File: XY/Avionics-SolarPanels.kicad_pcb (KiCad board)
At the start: 4 copper layers, 82 x 100 mm, 202 parts, among them J1 200528-0100, J2 200528-0100, Q1 IRLML2803, Q17 NX3008NBKS, Q18 MBT2222ADW1T1, Q19 NX3008NBKS, Q2 SiRA99DP, Q20 MBT2222ADW1T1, Q21 NX3008NBKS, Q22 MBT2222ADW1T1, Q23 NX3008NBKS, Q24 MBT2222ADW1T1, Q25 NX3008NBKS, Q26 MBT2222ADW1T1, Q3 SiRA99DP, Q4 SiRA99DP, Q5 SiRA99DP, Q7 NX3008NBKS, Q8 MBT2222ADW1T1, U1 LTC4412xS6, U10 LTC3130, U11 LTC3130, U12 LTC3130, U13 ADM1176-1ARMZ-R7, U2 DRV8235RTER, U4 LTC4412xS6, U5 OPT4003DNPRQ1, U6 USBLC6-2P6, U8 LTC4412xS6

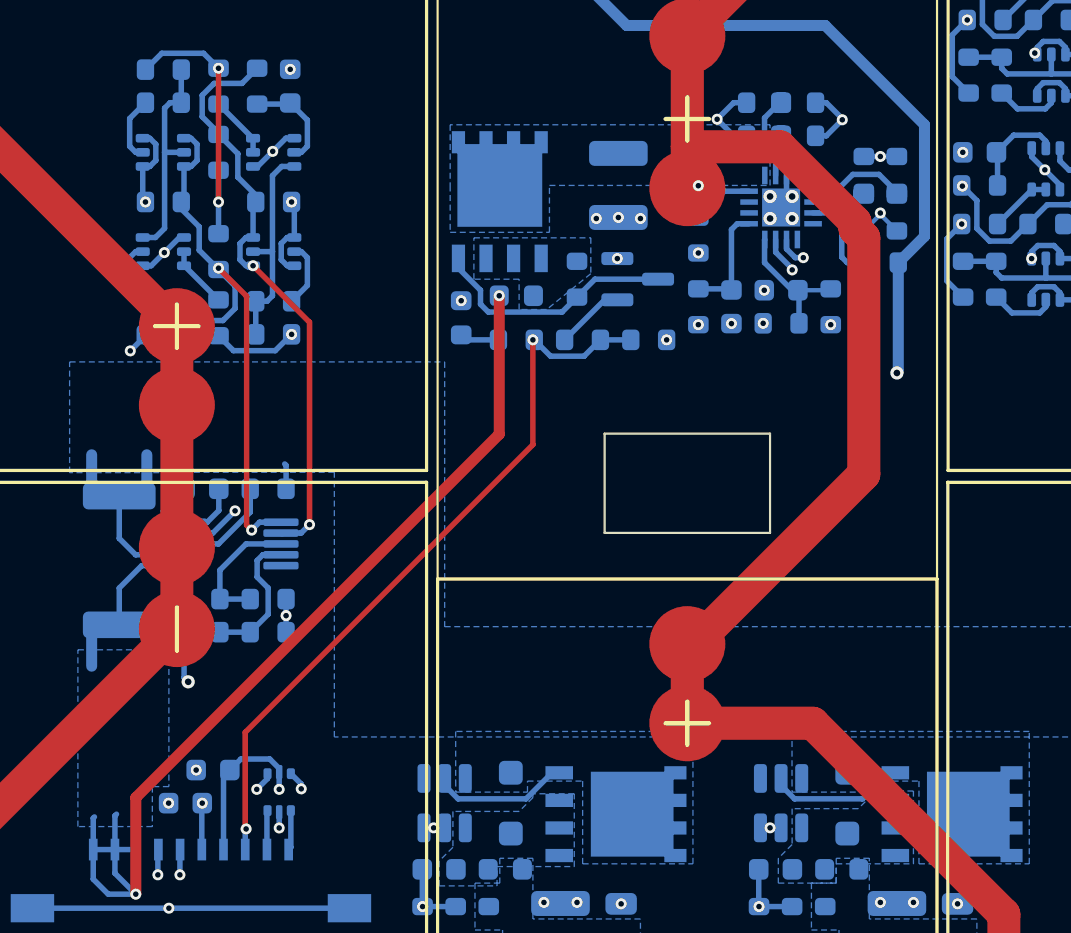
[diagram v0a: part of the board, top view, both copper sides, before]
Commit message: Increased usbc connnector size
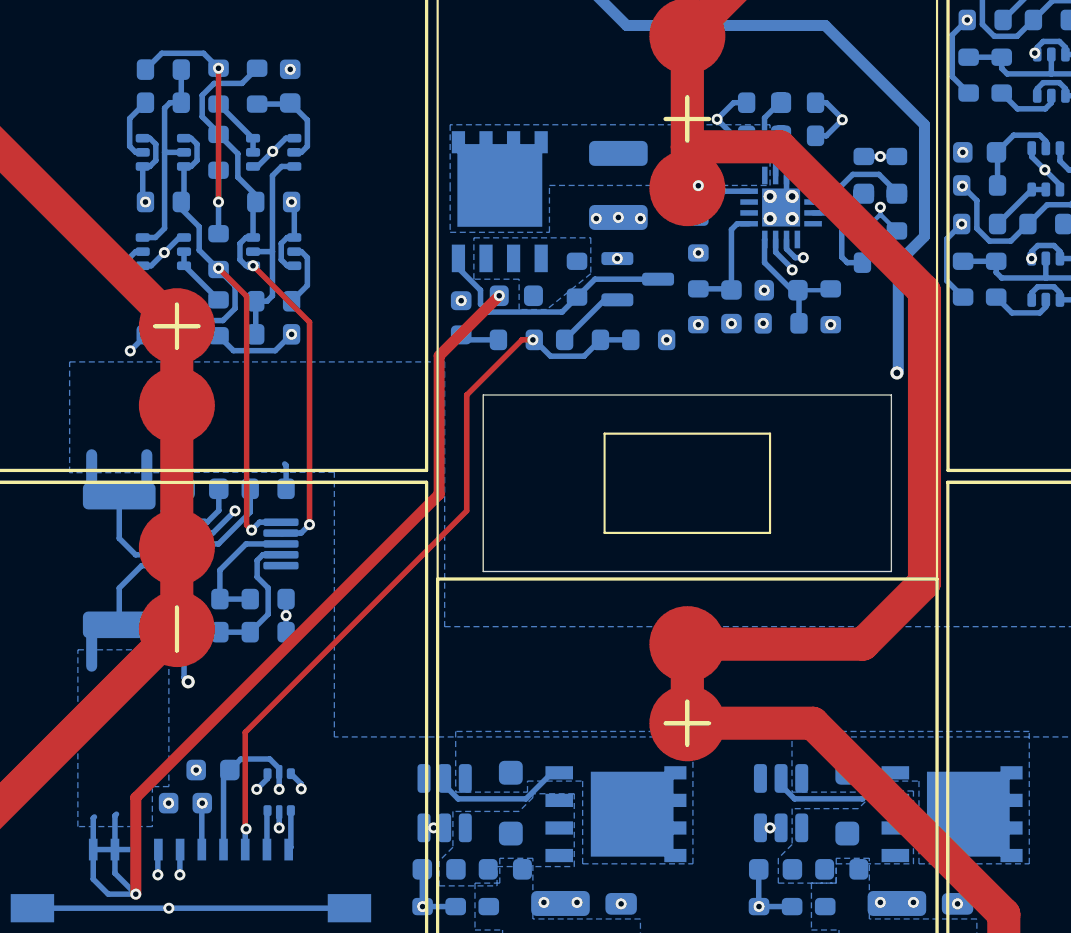
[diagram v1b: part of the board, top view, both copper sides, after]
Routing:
- net Net-(D3-K): track 140.4 -> 147.2 mm
- net PERI_3V3: track 99.6 -> 98.8 mm
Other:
- outline, holes or cut-outs redrawn
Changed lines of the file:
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@@
 		(tags "capacitor")
 		(property "Reference" "C22"
-			(at 3.302 -0.254 90)
+			(at 2.54 0 90)
 			(layer "B.SilkS")
 			(effects
@@
 		(tags "capacitor")
 		(property "Reference" "C28"
-			(at 0 -3.302 0)
+			(at 0 -2.794 0)
 			(layer "B.SilkS")
 			(effects
@@
 		(tags "resistor")
 		(property "Reference" "R53"
-			(at 3.048 0 90)
+			(at 2.54 0 90)
 			(layer "B.SilkS")
 			(effects
@@
 		(tags "resistor")
 		(property "Reference" "R32"
-			(at 3.302 -0.254 90)
+			(at 2.54 0 90)
 			(layer "B.SilkS")
 			(effects
@@
 		(tags "resistor")
 		(property "Reference" "R37"
-			(at 0 -1.778 0)
+			(at 0 -1.524 0)
 			(layer "B.SilkS")
 			(effects
@@
 		(tags "resistor")
 		(property "Reference" "R52"
-			(at 0 3.302 0)
+			(at 0 2.286 0)
 			(layer "B.SilkS")
 			(effects
@@
 		(tags "resistor")
 		(property "Reference" "R39"
-			(at 0 -1.778 0)
+			(at 0 -1.524 0)
 			(layer "B.SilkS")
 			(effects
@@
 	)
 	(gr_line
-		(start 156.21 100.584)
-		(end 148.59 100.584)
+		(start 161.798 98.806)
+		(end 143.002 98.806)
 		(stroke
 			(width 0.05)
@@
 	)
 	(gr_line
-		(start 148.59 100.584)
-		(end 148.59 105.156)
+		(start 143.002 98.806)
+		(end 143.002 106.934)
 		(stroke
 			(width 0.05)
@@
 	)
 	(gr_line
-		(start 148.59 105.156)
-		(end 156.21 105.156)
+		(start 143.002 106.934)
+		(end 161.798 106.934)
 		(stroke
 			(width 0.05)
@@
 	)
 	(gr_line
-		(start 156.21 105.156)
-		(end 156.21 100.584)
+		(start 161.798 106.934)
+		(end 161.798 98.806)
 		(stroke
 			(width 0.05)
@@
 	)
 	(via
-		(at 161.29 90.424)
+		(at 161.290001 90.157072)
 		(size 0.508)
 		(drill 0.254)
@@
 	)
 	(segment
+		(start 161.290001 90.157072)
+		(end 161.29 90.157073)
+		(width 0.2032)
+		(layer "B.Cu")
+		(net 40)
+	)
+	(segment
 		(start 161.29 90.487)
 		(end 160.528 91.249)
@@
 	)
 	(segment
-		(start 161.29 90.424)
-		(end 161.29 90.487)
-		(width 0.2032)
-		(layer "B.Cu")
-		(net 40)
-	)
-	(segment
 		(start 177.355 90.932)
 		(end 178.04386 90.24314)
@@
 	)
 	(segment
+		(start 161.29 90.157073)
+		(end 161.29 90.487)
+		(width 0.2032)
+		(layer "B.Cu")
+		(net 40)
+	)
+	(segment
 		(start 178.04386 88.31886)
 		(end 177.292 87.567)
@@
 	)
 	(segment
-		(start 152.703846 110.2786)
-		(end 160.528 102.454446)
-		(width 1.524)
-		(layer "F.Cu")
-		(net 46)
-	)
-	(segment
-		(start 160.528 102.454446)
-		(end 160.528 91.564776)
+		(start 160.4854 110.2786)
+		(end 163.322 107.442)
 		(width 1.524)
 		(layer "F.Cu")
@@
 	)
 	(segment
-		(start 160.528 91.564776)
-		(end 160.12414 91.160916)
-		(width 1.524)
-		(layer "F.Cu")
-		(net 46)
-	)
-	(segment
 		(start 167.728 147.574)
 		(end 166.978 146.824)
@@
 	)
 	(segment
-		(start 152.4 87.376)
-		(end 152.4 82.2786)
+		(start 152.4 110.2786)
+		(end 160.4854 110.2786)
 		(width 1.524)
 		(layer "F.Cu")
@@
 	)
 	(segment
-		(start 160.12414 91.160916)
-		(end 160.12414 90.839522)
+		(start 152.4 87.376)
+		(end 152.4 82.2786)
 		(width 1.524)
 		(layer "F.Cu")
@@
 	)
 	(segment
-		(start 160.12414 90.839522)
-		(end 156.660618 87.376)
+		(start 163.322 107.442)
+		(end 163.322 94.037382)
+		(width 1.524)
+		(layer "F.Cu")
+		(net 46)
+	)
+	(segment
+		(start 156.660618 87.376)
+		(end 152.4 87.376)
 		(width 1.524)
 		(layer "F.Cu")
@@
 	)
 	(segment
-		(start 156.660618 87.376)
-		(end 152.4 87.376)
+		(start 163.322 94.037382)
+		(end 156.660618 87.376)
 		(width 1.524)
 		(layer "F.Cu")
@@
 	)
 	(segment
-		(start 152.4 110.2786)
-		(end 152.703846 110.2786)
-		(width 1.524)
-		(layer "F.Cu")
-		(net 46)
-	)
-	(segment
 		(start 166.978 146.824)
 		(end 166.978 122.723026)
@@
 	)
 	(segment
-		(start 149.098 97.79)
-		(end 145.034 101.854)
+		(start 162.052 97.79)
+		(end 162.56 98.298)
 		(width 0.508)
 		(layer "In2.Cu")
@@
 	)
 	(segment
-		(start 140.988553 118.0815)
-		(end 130.5405 118.0815)
+		(start 162.56 107.442)
+		(end 151.9205 118.0815)
 		(width 0.508)
 		(layer "In2.Cu")
@@
 	)
 	(segment
-		(start 145.034 114.046)
-		(end 140.993526 118.086474)
+		(start 162.56 98.298)
+		(end 162.56 107.442)
 		(width 0.508)
 		(layer "In2.Cu")
@@
 	)
 	(segment
-		(start 140.993526 118.086474)
-		(end 140.988553 118.0815)
+		(start 151.9205 118.0815)
+		(end 130.5405 118.0815)
 		(width 0.508)
 		(layer "In2.Cu")
@@
 	)
 	(segment
-		(start 145.034 101.854)
-		(end 145.034 114.046)
-		(width 0.508)
-		(layer "In2.Cu")
-		(net 48)
-	)
-	(segment
-		(start 162.052 97.79)
-		(end 149.098 97.79)
-		(width 0.508)
-		(layer "In2.Cu")
-		(net 48)
-	)
-	(segment
 		(start 145.796 77.978)
 		(end 149.606 81.788)
@@
 	)
 	(segment
-		(start 127 117.348)
-		(end 143.7385 100.6095)
+		(start 140.97 97.0025)
+		(end 143.7385 94.234)
 		(width 0.508)
 		(layer "F.Cu")
@@
 	)
 	(segment
-		(start 127 121.793)
-		(end 127 117.348)
+		(start 140.97 103.378)
+		(end 140.97 97.0025)
 		(width 0.508)
 		(layer "F.Cu")
@@
 	)
 	(segment
-		(start 143.7385 100.6095)
-		(end 143.7385 94.234)
+		(start 127 117.348)
+		(end 140.97 103.378)
+		(width 0.508)
+		(layer "F.Cu")
+		(net 53)
+	)
+	(segment
+		(start 127 121.793)
+		(end 127 117.348)
 		(width 0.508)
 		(layer "F.Cu")
@@
 	(segment
 		(start 132.04 114.34)
-		(end 145.288 101.092)
+		(end 142.24 104.14)
+		(width 0.254)
+		(layer "F.Cu")
+		(net 101)
+	)
+	(segment
+		(start 142.24 104.14)
+		(end 142.24 98.806)
 		(width 0.254)
 		(layer "F.Cu")
@@
 	)
 	(segment
-		(start 145.288 101.092)
+		(start 144.78 96.266)
 		(end 145.288 96.266)
 		(width 0.254)
 		(layer "F.Cu")
+		(net 101)
+	)
+	(segment
+		(start 142.24 98.806)
+		(end 144.78 96.266)
+		(width 0.254)
+		(layer "F.Cu")

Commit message: Routing modifications
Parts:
- removed C36: 0.1uF, Capacitor_SMD:C_0603_1608Metric
- moved R102 4.82 mm to (152.9, 61.0), turned to 0 degrees
- moved R103 4.82 mm to (152.9, 65.5), turned to 180 degrees
- moved R104 3.39 mm to (150.1, 63.2)
- moved F1 2.34 mm to (149.4, 61.0), turned to 180 degrees
- moved R105 1.93 mm to (148.6, 63.2)
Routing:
- net GND: track 136.1 -> 120.7 mm, vias 78 -> 77
- net /Light Sensor/LS_3V3: track 71.9 -> 63.6 mm
- net /Light Sensor/ADDR_LS: track 4.84 -> 12.5 mm
- net /Light Sensor/SDA_LS: track 45.6 -> 38.4 mm
- net /Light Sensor/SCL_LS: track 47.5 -> 43.7 mm
- net PERI_3V3: track 98.8 -> 100.2 mm

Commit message: Pushed uncommitted changes
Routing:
- net GND: track 120.7 -> 122.5 mm, vias 77 -> 76
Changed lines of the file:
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@@
 		(tags "resistor")
 		(property "Reference" "R102"
-			(at 1.524 -3.048 360)
+			(at 1.524 -3.048 0)
 			(layer "F.SilkS")
 			(effects
@@
 		)
 		(property "Value" "0R"
-			(at 0 1.43 360)
+			(at 0 1.43 0)
 			(layer "F.Fab")
 			(effects
@@
 		)
 		(fp_text user "${REFERENCE}"
-			(at 0 0 360)
+			(at 0 0 0)
 			(layer "F.Fab")
 			(effects
@@
 		(tags "fuse")
 		(property "Reference" "F1"
-			(at 2.54 0 360)
+			(at 2.54 0 0)
 			(layer "F.SilkS")
 			(effects
@@
 		)
 		(property "Value" "100mA"
-			(at 0 1.43 360)
+			(at 0 1.43 0)
 			(layer "F.Fab")
 			(effects
@@
 		)
 		(fp_text user "${REFERENCE}"
-			(at 0 0 360)
+			(at 0 0 0)
 			(layer "F.Fab")
 			(effects
@@
 		(tags "resistor")
 		(property "Reference" "R103"
-			(at -1.016 -3.048 360)
+			(at -1.016 -3.048 0)
 			(layer "F.SilkS")
 			(effects
@@
 		)
 		(property "Value" "0R"
-			(at 0 1.43 360)
+			(at 0 1.43 0)
 			(layer "F.Fab")
 			(effects
@@
 		)
 		(fp_text user "${REFERENCE}"
-			(at 0 0 360)
+			(at 0 0 0)
 			(layer "F.Fab")
 			(effects
@@
 	)
 	(via
-		(at 152.908 89.167)
-		(size 0.508)
-		(drill 0.254)
-		(layers "F.Cu" "B.Cu")
-		(net 1)
-	)
-	(via
 		(at 175.514 128.524)
 		(size 0.508)
@@
 	(via
 		(at 156.21 89.662)
-		(size 0.6096)
-		(drill 0.3048)
+		(size 0.508)
+		(drill 0.254)
 		(layers "F.Cu" "B.Cu")
 		(net 1)
@@
 	(via
 		(at 157.226 90.678)
-		(size 0.6096)
-		(drill 0.3048)
+		(size 0.508)
+		(drill 0.254)
 		(layers "F.Cu" "B.Cu")
 		(net 1)
@@
 	(via
 		(at 156.21 90.678)
-		(size 0.6096)
-		(drill 0.3048)
+		(size 0.508)
+		(drill 0.254)
 		(layers "F.Cu" "B.Cu")
 		(net 1)
@@
 	(via
 		(at 178.054 93.599)
-		(size 0.6096)
-		(drill 0.3048)
+		(size 0.508)
+		(drill 0.254)
 		(layers "F.Cu" "B.Cu")
 		(net 1)
@@
 	(via
 		(at 129.413 112.014)
-		(size 0.6096)
-		(drill 0.3048)
+		(size 0.508)
+		(drill 0.254)
 		(layers "F.Cu" "B.Cu")
 		(net 1)
@@
 	(via
 		(at 157.226 89.662)
-		(size 0.6096)
-		(drill 0.3048)
+		(size 0.508)
+		(drill 0.254)
 		(layers "F.Cu" "B.Cu")
 		(net 1)
@@
 	)
 	(segment
+		(start 150.333 90.678)
+		(end 151.511 89.5)
+		(width 0.2032)
+		(layer "B.Cu")
+		(net 1)
+	)
+	(segment
 		(start 171.262 118.7395)
 		(end 171.704 118.7395)
@@
 	)
 	(segment
+		(start 150.241 90.678)
+		(end 150.333 90.678)
+		(width 0.2032)
+		(layer "B.Cu")
+		(net 1)
+	)
+	(segment
 		(start 147.238 128.274)
 		(end 145.538 128.274)
@@
 	)
 	(segment
-		(start 154.432 60.198)
-		(end 161.417 67.183)
-		(width 0.2032)
-		(layer "F.Cu")
-		(net 29)
-	)
-	(segment
-		(start 150.114 62.421)
-		(end 151.450299 62.421)
+		(start 153.162 60.198)
+		(end 152.908 60.452)
 		(width 0.2032)
 		(layer "F.Cu")
@@
 	)
 	(segment
-		(start 153.162 60.198)
-		(end 154.432 60.198)
+		(start 154.432 60.198)
+		(end 153.162 60.198)
 		(width 0.2032)
 		(layer "F.Cu")
@@
 	)
 	(segment
-		(start 150.1395 60.96)
-		(end 150.1395 62.3955)
+		(start 151.779999 62.596001)
+		(end 151.6253 62.596001)
 		(width 0.2032)
 		(layer "F.Cu")
@@
 	)
 	(segment
-		(start 151.779999 62.596001)
+		(start 152.908 60.452)
 		(end 152.908 61.468)
 		(width 0.2032)
@@
 	)
 	(segment
-		(start 152.908 61.468)
-		(end 152.908 60.452)
+		(start 150.114 62.421)
+		(end 151.450299 62.421)
 		(width 0.2032)
 		(layer "F.Cu")
@@
 	)
 	(segment
-		(start 152.908 60.452)
-		(end 153.162 60.198)
+		(start 150.1395 60.96)
+		(end 150.1395 62.3955)
 		(width 0.2032)
 		(layer "F.Cu")
@@
 	(segment
 		(start 161.417 67.183)
-		(end 161.417 69.977)
+		(end 154.432 60.198)
+		(width 0.2032)
+		(layer "F.Cu")
+		(net 29)
+	)
+	(segment
+		(start 161.417 69.723)
+		(end 161.417 67.183)
 		(width 0.2032)
 		(layer "F.Cu")
@@
 	)
 	(segment
-		(start 151.6253 62.596001)
+		(start 152.908 61.468)
 		(end 151.779999 62.596001)
 		(width 0.2032)
@@
 	)
 	(via
-		(at 161.417 69.977)
+		(at 161.417 69.723)
 		(size 0.508)
 		(drill 0.254)
@@
 	)
 	(segment
+		(start 161.671 69.977)
+		(end 164.592 69.977)
+		(width 0.254)
+		(layer "In2.Cu")
+		(net 29)
+	)
+	(segment
+		(start 164.592 69.977)
+		(end 165.88486 71.26986)
+		(width 0.254)
+		(layer "In2.Cu")
+		(net 29)
+	)
+	(segment
 		(start 165.291 81.534)
 		(end 171.45 81.534)
@@
 	)
 	(segment
-		(start 165.88486 80.94014)
-		(end 165.291 81.534)
+		(start 161.417 69.723)
+		(end 161.671 69.977)
 		(width 0.254)
 		(layer "In2.Cu")
@@
 	)
 	(segment
-		(start 171.45 81.534)
-		(end 170.919 81.003)
+		(start 165.88486 80.94014)
+		(end 165.291 81.534)
 		(width 0.254)
 		(layer "In2.Cu")
@@
 	)
 	(segment
-		(start 170.919 81.003)
-		(end 170.919 77.949052)
+		(start 171.45 81.534)
+		(end 170.919 81.003)
 		(width 0.254)
 		(layer "In2.Cu")
@@
 	)
 	(segment
-		(start 161.417 69.977)
-		(end 164.592 69.977)
+		(start 170.919 81.003)
+		(end 170.919 77.949052)
 		(width 0.254)
 		(layer "In2.Cu")
@@
 	)
 	(segment
-		(start 164.592 69.977)
-		(end 165.88486 71.26986)
-		(width 0.254)
-		(layer "In2.Cu")
-		(net 29)
-	)
-	(segment
 		(start 171.230052 77.638)
 		(end 177.015 77.638)
@@
 	(via
 		(at 162.052 97.79)
-		(size 0.6096)
-		(drill 0.3048)
+		(size 0.508)
+		(drill 0.254)
 		(layers "F.Cu" "B.Cu")
 		(net 48)

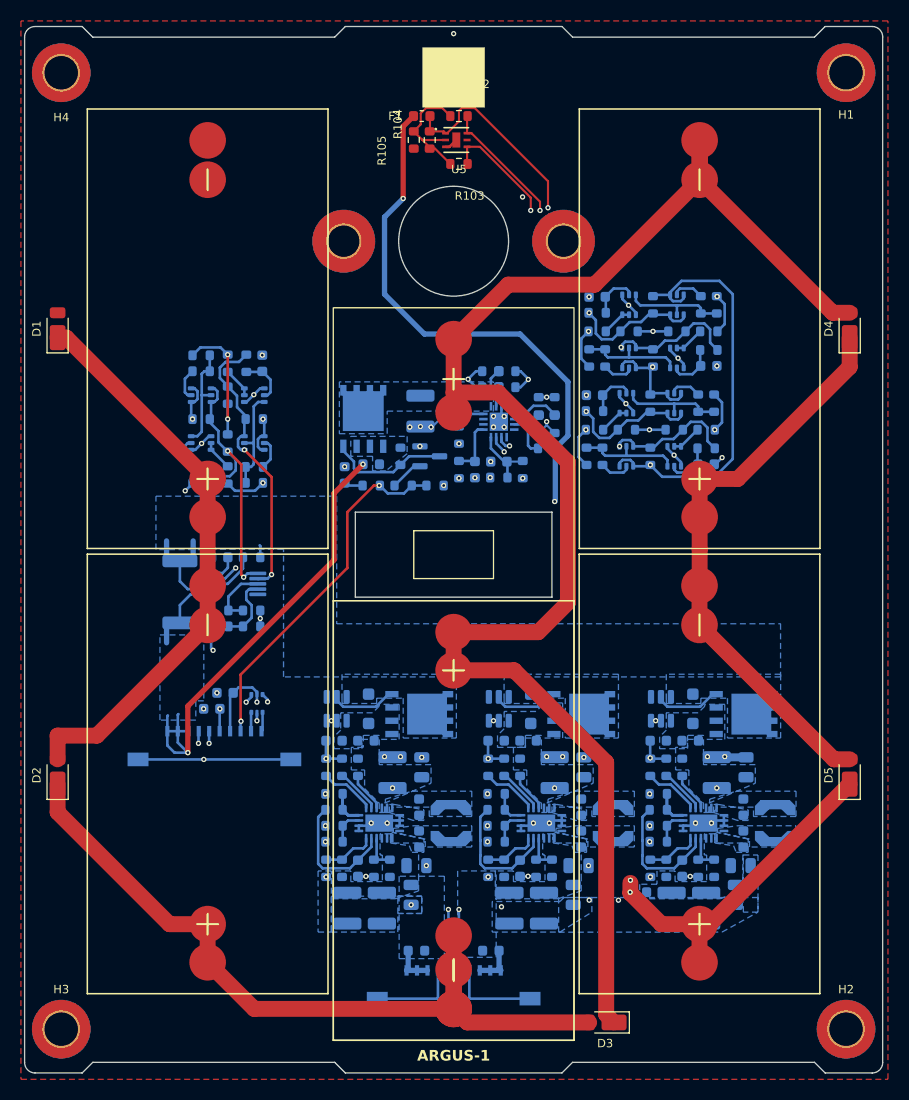
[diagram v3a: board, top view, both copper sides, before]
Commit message: Updated silkscreen and jumpers for mainboard compatability
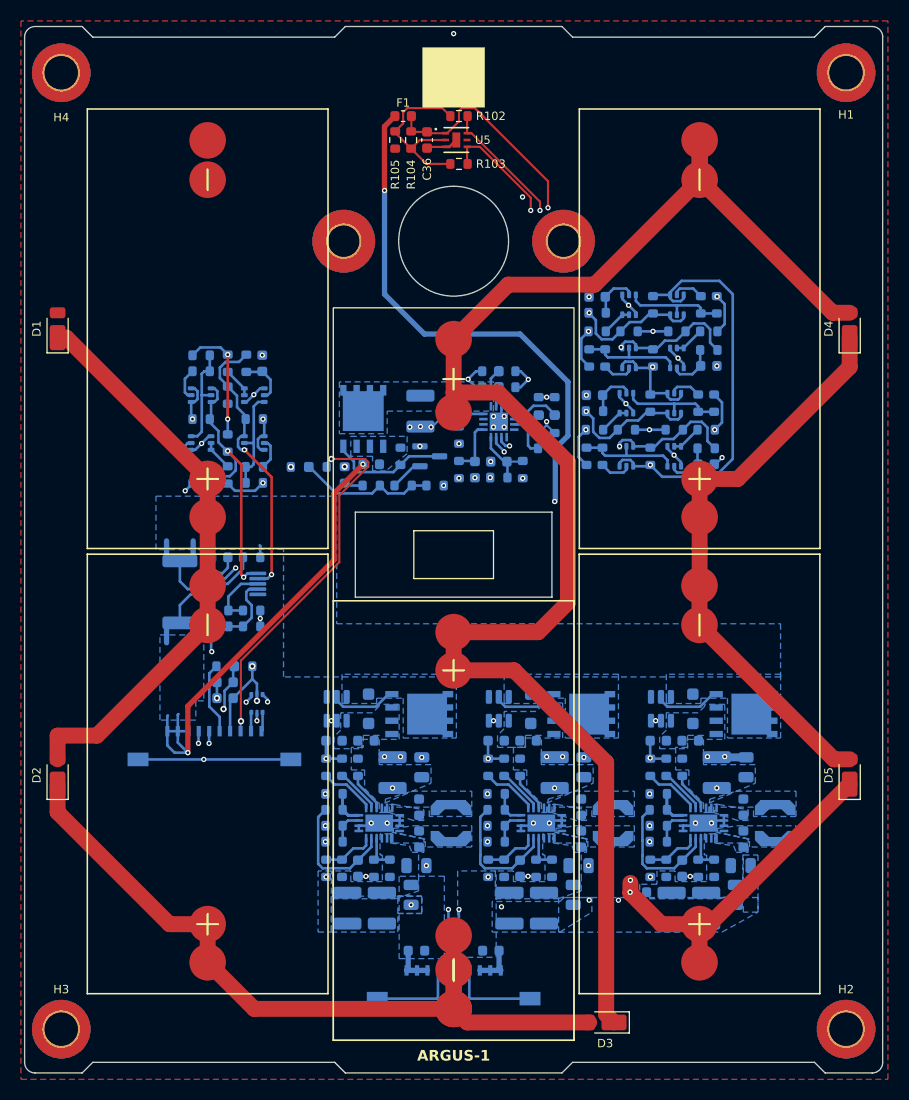
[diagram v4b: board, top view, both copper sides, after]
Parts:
- added C36: 0.1uF, Capacitor_SMD:C_0603_1608Metric, F.Cu at (149.9, 63.2)
- added R40: 0R, Resistor_SMD:R_0603_1608Metric, B.Cu at (139.4, 94.5)
- added R41: 0R, Resistor_SMD:R_0603_1608Metric, B.Cu at (137.7, 94.5)
- added R42: 0R, Resistor_SMD:R_0603_1608Metric, B.Cu at (130.6, 113.5)
- added R43: 0R, Resistor_SMD:R_0603_1608Metric, B.Cu at (132.3, 113.5)
- R17, R19, R21: value 107K -> 126k
- R22, R23, R24: value 127k -> 182k
- SC1, SC2, SC4, SC5, SC6: value SM141K06L -> SM141K06TF
- moved C25 2.84 mm to (130.6, 115.1)
- moved F1 1.78 mm to (147.6, 61.0)
- moved R104 1.78 mm to (148.3, 63.2)
- moved R105 1.78 mm to (146.8, 63.2)
- moved C24 0.51 mm to (130.6, 116.6)
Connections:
- J2 pad 3: COIL_DRIVER_EN -> /Interfaces/COIL_DRIVER_EN_OR_MAIN_3V3
- J2 pad 5: PERI_3V3 -> /Interfaces/PERI_3V3_OR_GND
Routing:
- net /Interfaces/COIL_DRIVER_EN_OR_MAIN_3V3: track 0.00 -> 35.6 mm, vias 0 -> 2
- net COIL_DRIVER_EN: track 34.4 -> 13.2 mm, vias 2 -> 0
- net /Interfaces/PERI_3V3_OR_GND: track 0.00 -> 6.89 mm
- net /Light Sensor/ADDR_LS: track 12.5 -> 17.4 mm
- net GND: track 122.5 -> 125.9 mm
- net MAIN_3V3: track 39.4 -> 41.3 mm, vias 11 -> 12
- net /Light Sensor/LS_3V3: track 63.4 -> 65.2 mm
- net PERI_3V3: track 100.2 -> 101.5 mm
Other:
- board text added: "ARGUS Cubesat Carnegie Mellon University X/Y Solar Panel v3"
- board text added: "CDR_EN"
- board text added: "M_3V3"
- board text added: "P_3V3"
- board text removed: "3.3V"
- board text removed: "ARGUS-1 Cubesat Carnegie Mellon University X/Y Solar Panel v1"
- board text removed: "COIL EN"
